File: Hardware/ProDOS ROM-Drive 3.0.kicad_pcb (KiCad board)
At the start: 2 copper layers, 85.7 x 54 mm, 17 parts, among them J1 Apple II Expansion Slot, U1 74LS00, U2 74LS32

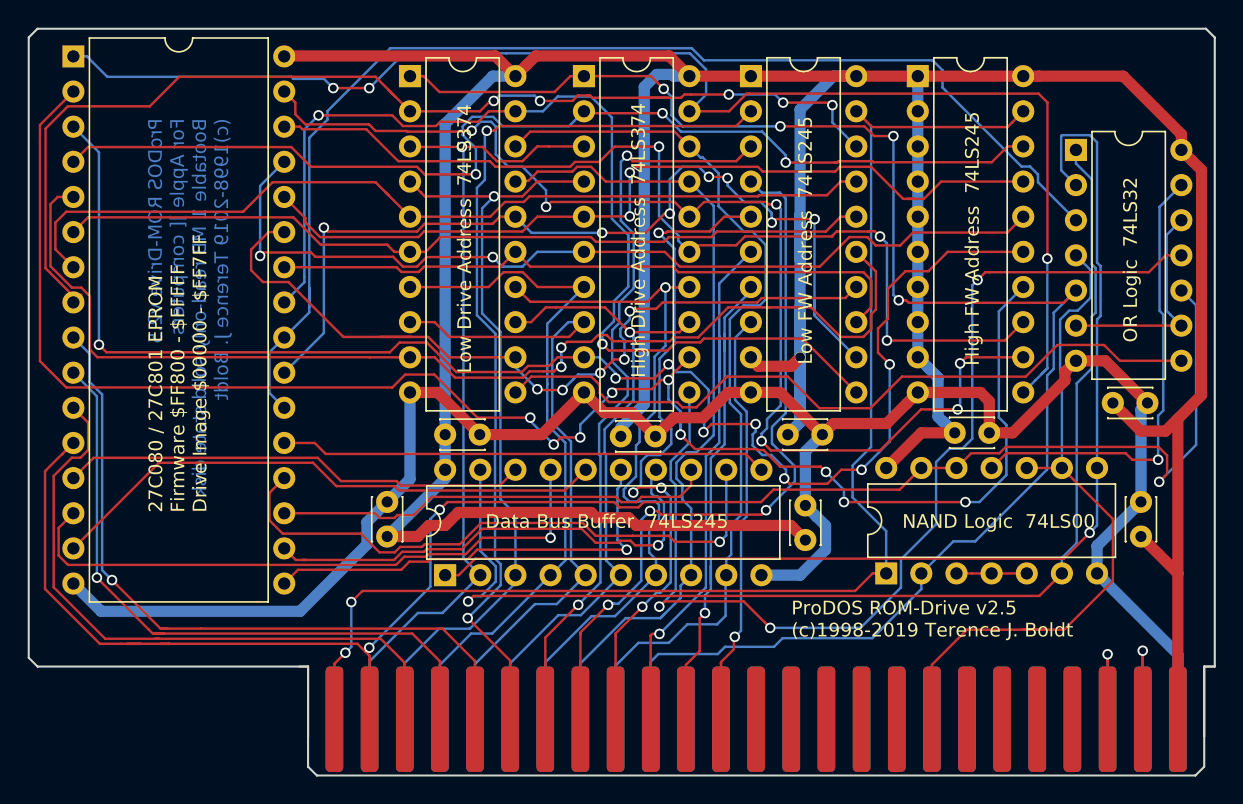
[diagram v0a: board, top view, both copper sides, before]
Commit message: Update hardware to use block 0001 for firmware
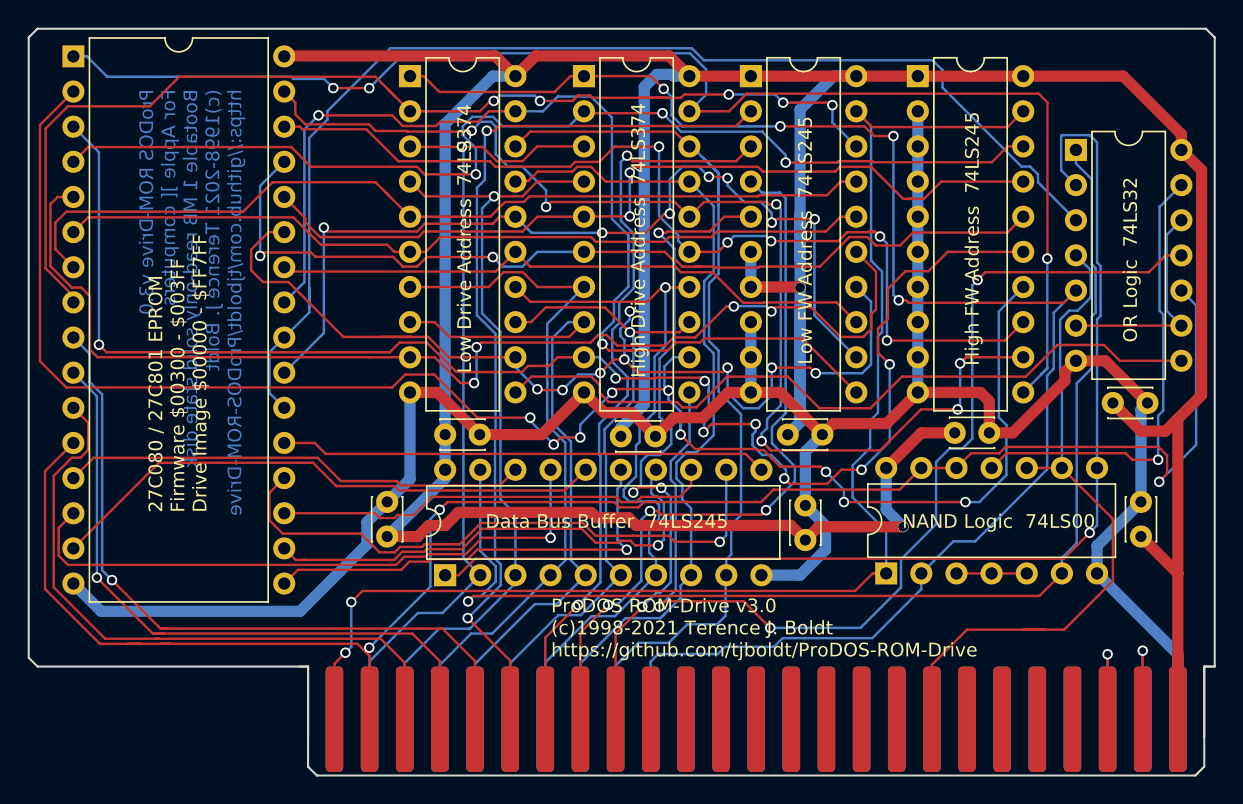
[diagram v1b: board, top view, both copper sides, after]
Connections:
- HiAddrBuffer1 pad 2: +5V -> GND
- HiAddrBuffer1 pad 3: +5V -> GND
- HiAddrBuffer1 pad 4: +5V -> GND
- HiAddrBuffer1 pad 5: +5V -> GND
- HiAddrBuffer1 pad 6: +5V -> GND
- HiAddrBuffer1 pad 7: +5V -> GND
- HiAddrBuffer1 pad 8: +5V -> GND
- HiAddrBuffer1 pad 9: +5V -> GND
- J1 pad 10: Net-(J1-Pad10) -> (no net)
- J1 pad 11: Net-(J1-Pad11) -> (no net)
- J1 pad 12: Net-(J1-Pad12) -> (no net)
- J1 pad 13: Net-(J1-Pad13) -> (no net)
- J1 pad 14: Net-(J1-Pad14) -> (no net)
- J1 pad 15: Net-(J1-Pad15) -> (no net)
- J1 pad 16: Net-(J1-Pad16) -> (no net)
- J1 pad 17: Net-(J1-Pad17) -> (no net)
- J1 pad 19: Net-(J1-Pad19) -> (no net)
- J1 pad 20: Net-(J1-Pad20) -> (no net)
- J1 pad 21: Net-(J1-Pad21) -> (no net)
- J1 pad 22: Net-(J1-Pad22) -> (no net)
- J1 pad 29: Net-(J1-Pad29) -> (no net)
- J1 pad 30: Net-(J1-Pad30) -> (no net)
- J1 pad 31: Net-(J1-Pad31) -> (no net)
- J1 pad 32: Net-(J1-Pad32) -> (no net)
- J1 pad 33: Net-(J1-Pad33) -> (no net)
- J1 pad 34: Net-(J1-Pad34) -> (no net)
- J1 pad 35: Net-(J1-Pad35) -> (no net)
- J1 pad 36: Net-(J1-Pad36) -> (no net)
- J1 pad 37: Net-(J1-Pad37) -> (no net)
- J1 pad 38: Net-(J1-Pad38) -> (no net)
- J1 pad 39: Net-(J1-Pad39) -> (no net)
- J1 pad 40: Net-(J1-Pad40) -> (no net)
- J1 pad 50: Net-(J1-Pad50) -> (no net)
- LowAddrBuffer1 pad 6: Net-(J1-Pad10) -> +5V
- LowAddrBuffer1 pad 7: Net-(J1-Pad11) -> +5V
- LowAddrBuffer1 pad 8: Net-(J1-Pad12) -> GND
- LowAddrBuffer1 pad 9: +5V -> GND
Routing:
- net Net-(J1-Pad10): track 40.5 -> 0.00 mm, vias 1 -> 0
- net Net-(J1-Pad11): track 35.7 -> 0.00 mm, vias 1 -> 0
- net Net-(J1-Pad12): track 30.3 -> 0.00 mm, vias 1 -> 0
- net GND: track 145.6 -> 171.0 mm
- net Net-(EPROM1-Pad27): track 59.6 -> 72.2 mm, vias 5 -> 8
- net +5V: track 300.2 -> 287.7 mm, vias 1 -> 2
- net Net-(EPROM1-Pad26): track 47.9 -> 44.6 mm
- net Net-(EPROM1-Pad30): track 70.3 -> 72.1 mm, vias 3 -> 5
- net Net-(DataBuffer1-Pad9): track 66.4 -> 67.7 mm
- net Net-(EPROM1-Pad8): track 81.7 -> 80.7 mm
- net Net-(HiAddrBuffer1-Pad19): track 96.9 -> 97.6 mm
- net Net-(DataBuffer1-Pad8): track 60.2 -> 60.7 mm
- net Net-(EPROM1-Pad29): track 67.1 -> 67.7 mm
- net Net-(EPROM1-Pad2): track 121.2 -> 121.8 mm
- net Net-(EPROM1-Pad5): track 83.0 -> 83.5 mm, vias 2 -> 4
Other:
- board text added: "27C080 / 27C801 EPROM Firmware $00300 - $003FF Drive Image $00000 - $FF7FF"
- board text added: "ProDOS ROM-Drive v3.0 (c)1998-2021 Terence J. Boldt https://github.com/tjboldt/ProDOS-ROM-Drive"
- board text added: "ProDOS ROM-Drive v3.0 For Apple ][ computers Bootable 1 MB read-only solid state disk (c)1998-2021 Terence J. Boldt https://github.com/tjboldt/ProDOS-ROM-Drive"
- board text removed: "27C080 / 27C801 EPROM Firmware $FF800 - $FFFFF Drive Image $00000 - $FF7FF"
- board text removed: "ProDOS ROM-Drive v2.5 (c)1998-2019 Terence J. Boldt"
- board text removed: "ProDOS ROM-Drive v2.5 For Apple ][ computers Bootable 1 MB read-only solid state disk (c)1998-2019 Terence J. Boldt"

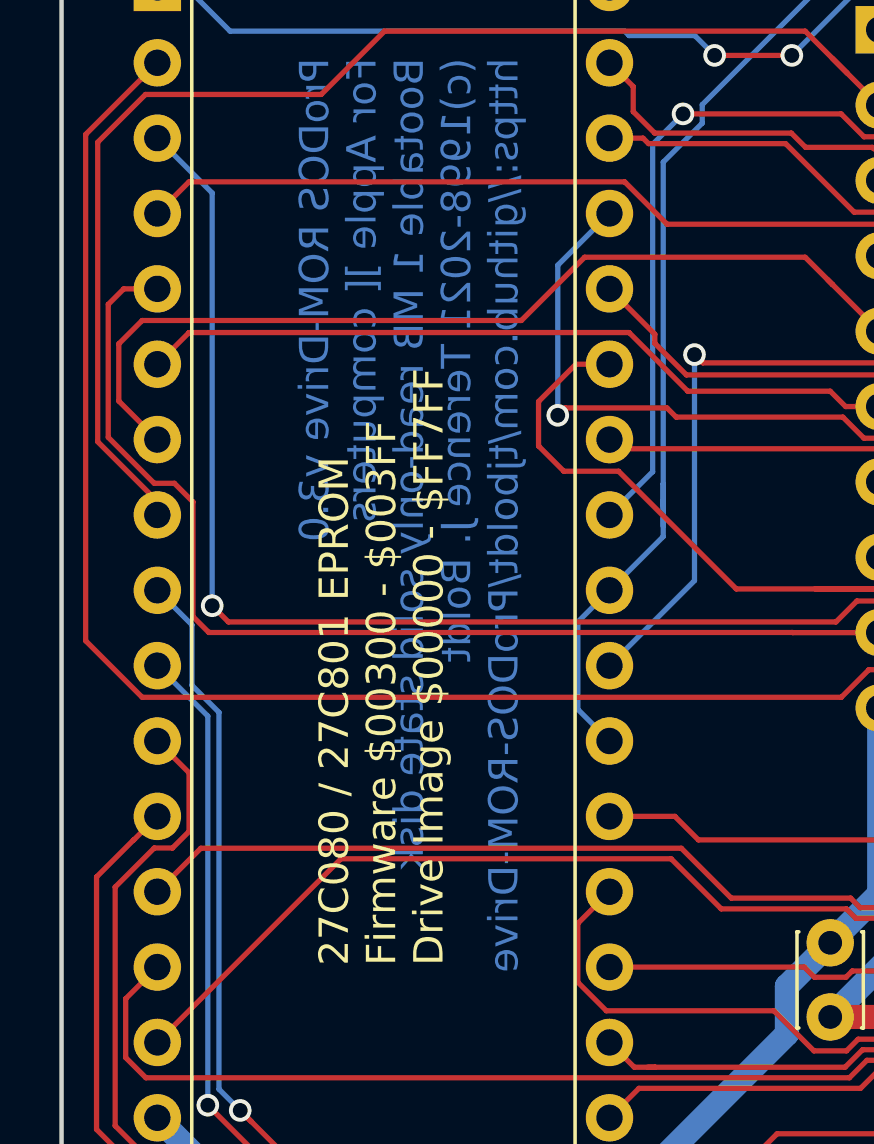
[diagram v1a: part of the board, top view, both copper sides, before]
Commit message: Update firmware source to be relocatable
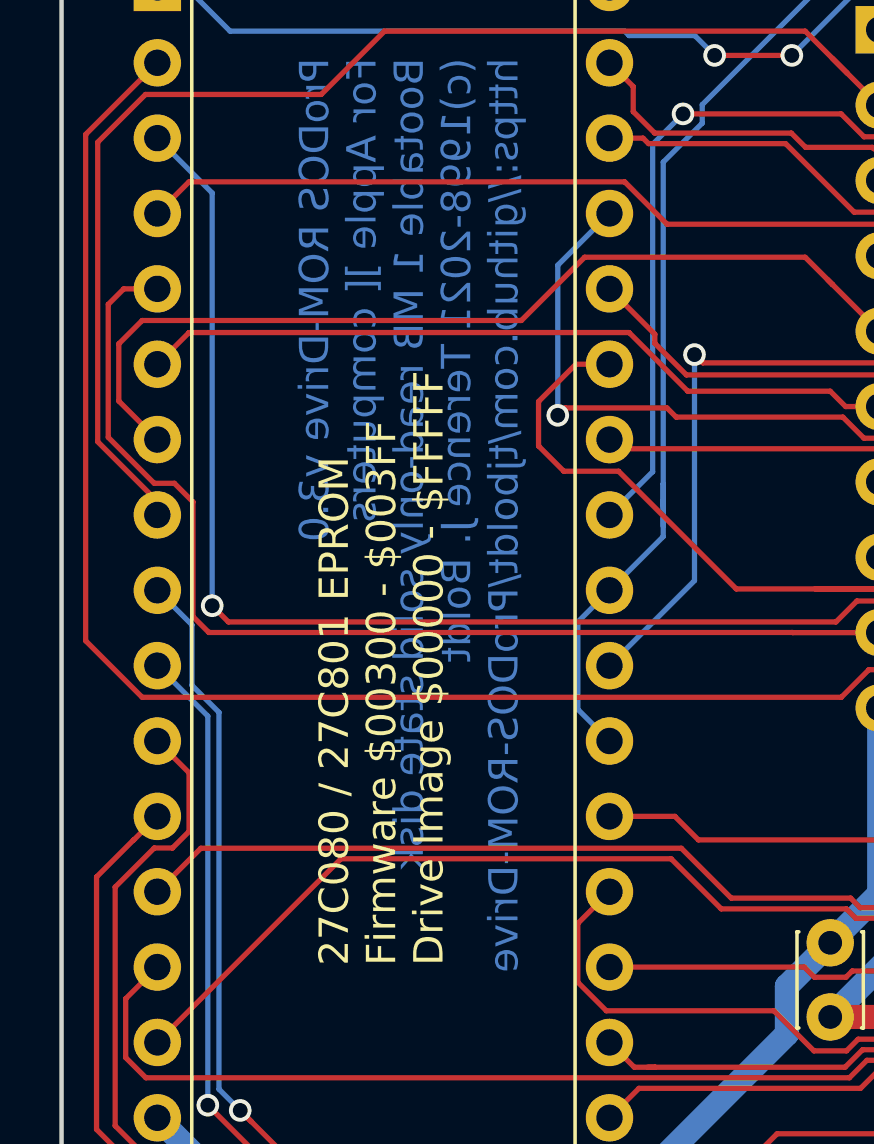
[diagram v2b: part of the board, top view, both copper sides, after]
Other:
- board text added: "27C080 / 27C801 EPROM Firmware $00300 - $003FF Drive Image $00000 - $FFFFF"
- board text removed: "27C080 / 27C801 EPROM Firmware $00300 - $003FF Drive Image $00000 - $FF7FF"
